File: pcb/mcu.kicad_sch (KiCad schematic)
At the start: 27 parts, among them SW1 PTS810, SW2 PTS810, U1 RP2040, U2 W25Q16JVSS, Y1 ABM8-272-T3

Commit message: add top level schem and cleanup
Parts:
- removed U1: RP2040, Package_DFN_QFN:QFN-56-1EP_7x7mm_P0.4mm_EP3.2x3.2mm, symbol MCU_RaspberryPi:RP2040
- removed U2: W25Q16JVSS, Package_SO:SOIC-8_5.3x5.3mm_P1.27mm, symbol Memory_Flash:W25Q16JVSS
- added U1: W25Q16JVSS, Package_SO:SOIC-8_5.3x5.3mm_P1.27mm, symbol Memory_Flash:W25Q16JVSS
- added U2: RP2040, Package_DFN_QFN:QFN-56-1EP_7x7mm_P0.4mm_EP3.2x3.2mm, symbol MCU_RaspberryPi:RP2040
- C1, C2: value 1u -> 100n; Manufacturer P/N GRM155Z71A105KE01J -> (none); Vendor DigiKey -> (none); Vendor P/N 490-GRM155Z71A105KE01JCT-ND -> (none)
- C11: value 100n -> 1u; Manufacturer P/N (none) -> GRM155Z71A105KE01J; Vendor (none) -> DigiKey; Vendor P/N (none) -> 490-GRM155Z71A105KE01JCT-ND
- C12: value 15p -> 1u; Manufacturer P/N GRM1555C1H150JA01D -> GRM155Z71A105KE01J; Vendor P/N 490-5888-1-ND -> 490-GRM155Z71A105KE01JCT-ND
- C13: value 15p -> 100n; Manufacturer P/N GRM1555C1H150JA01D -> (none); Vendor DigiKey -> (none); Vendor P/N 490-5888-1-ND -> (none)
- C4, C5: value 100n -> 15p; Manufacturer P/N (none) -> GRM1555C1H150JA01D; Vendor (none) -> DigiKey; Vendor P/N (none) -> 490-5888-1-ND
- R1: value 1k -> 10k; Manufacturer P/N RC0402FR-071KL -> RC0402FR-0710KL; Vendor P/N 311-1.00KLRCT-ND -> 311-10.0KLRCT-ND
- R2: value 10k -> 1k; Manufacturer P/N RC0402FR-0710KL -> RC0402FR-071KL; Vendor P/N 311-10.0KLRCT-ND -> 311-1.00KLRCT-ND; now fitted
- R3: value 1k -> 10k; Manufacturer P/N RC0402FR-071KL -> RC0402FR-0710KL; Vendor P/N 311-1.00KLRCT-ND -> 311-10.0KLRCT-ND; now not fitted
- R5: value 27.4 -> 1k; Manufacturer P/N RC0402FR-0727R4L -> RC0402FR-071KL; Vendor P/N YAG3085CT-ND -> 311-1.00KLRCT-ND
- R6: value 10k -> 27.4; Manufacturer P/N RC0402FR-0710KL -> RC0402FR-0727R4L; Vendor P/N 311-10.0KLRCT-ND -> YAG3085CT-ND
- R7, R8: value 2k -> 4.7k
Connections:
- net +1.1V: now also C12.1, C13.1, C14.1, U2.23 (DVDD), U2.45 (VREG_VOUT), U2.50 (DVDD); no longer C1.1, C3.1, C4.1
- net +3.3V: now also C1.1, C3.1, R1.2, R3.1, U1.8 (VCC), U2.1 (IOVDD), U2.10 (IOVDD), U2.22 (IOVDD), U2.33 (IOVDD), U2.42 (IOVDD), U2.43 (ADC_AVDD), U2.44 (VREG_VIN), U2.48 (USB_VDD), U2.49 (IOVDD); no longer C14.1, C5.1, R2.1, R6.2
- net GND: now also C12.2, C13.2, C4.1, C5.1, U1.4 (GND), U2.19 (TESTEN), U2.57 (GND); no longer C12.1, C13.1, C4.2, C5.2
- net I2C.SCL: now also U2.16 (GPIO13)
- net I2C.SDA: now also U2.15 (GPIO12)
- net QSPI_CLK: now also U1.6 (CLK), U2.52 (QSPI_SCLK)
- net QSPI_SD0: now also U1.5 (DI/IO_{0}), U2.53 (QSPI_SD0)
- net QSPI_SD1: now also U1.2 (DO/IO_{1}), U2.55 (QSPI_SD1)
- net QSPI_SD2: now also U1.3 (~{WP}/IO_{2}), U2.54 (QSPI_SD2)
- net QSPI_SD3: now also U1.7 (~{HOLD}/~{RESET}/IO_{3}), U2.51 (QSPI_SD3)
- net SWD.CLK: now also U2.24 (SWCLK)
- net SWD.DIO: now also U2.25 (SWDIO)
- net USB.DP: now also R6.1; no longer R5.1
- net gp_btn_a: now also U2.38 (GPIO26/ADC0)
- net gp_btn_b: now also U2.39 (GPIO27/ADC1)
- net gp_led_a: now also U2.40 (GPIO28/ADC2)
- net gp_led_b: now also U2.41 (GPIO29/ADC3)
- net hall_int: now also U2.2 (GPIO0)
- net ind_led0: now also U2.7 (GPIO5)
- net ind_led1: now also U2.8 (GPIO6)
- net ind_led2: now also U2.9 (GPIO7)
- net temp_int: now also U2.3 (GPIO1)
- net ~{QSPI_CS}: now also R2.1, R3.2, U1.1 (~{CS}), U2.56 (~{QSPI_SS}); no longer R2.2, R3.1
- net ~{RESET}: now also R1.1, U2.26 (RUN); no longer R6.1
- net ~{USB_BOOT}: now also R2.2; no longer R3.2
- net at Y1.1: now also C4.2, U2.20 (XIN); no longer C12.2
- net at R4.2: now also U2.46 (USB_DM)
- net at R5.2: now also C5.2, Y1.3
- new net: R5.1, U2.21 (XOUT)
- new net: R6.2, U2.47 (USB_DP)
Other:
- title: (none) -> MCU

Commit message: cleanup routing
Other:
- moved on the sheet: C1, R1, R2, R3, SW1, SW2, U1

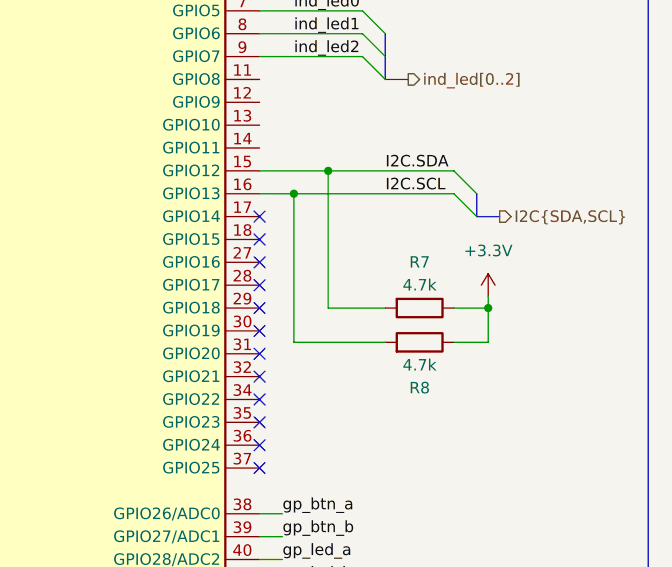
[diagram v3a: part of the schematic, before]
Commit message: custom symbols for all ics
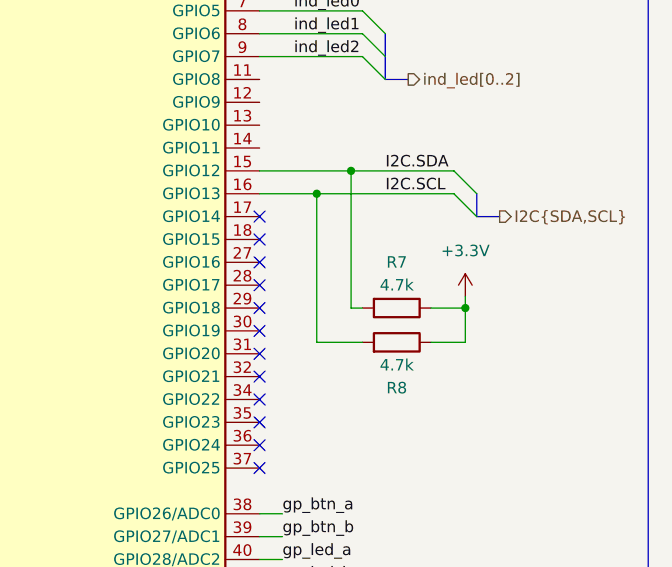
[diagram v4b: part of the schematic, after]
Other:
- moved on the sheet: R7, R8
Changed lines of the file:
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@@
 	)
 	(junction
-		(at 241.3 97.79)
+		(at 243.84 97.79)
 		(diameter 0)
 		(color 0 0 0 0)
@@
 	)
 	(junction
-		(at 237.49 100.33)
+		(at 240.03 100.33)
 		(diameter 0)
 		(color 0 0 0 0)
@@
 	)
 	(junction
-		(at 259.08 113.03)
+		(at 256.54 113.03)
 		(diameter 0)
 		(color 0 0 0 0)
@@
 	(wire
 		(pts
-			(xy 259.08 113.03) (xy 259.08 116.84)
+			(xy 256.54 113.03) (xy 256.54 116.84)
 		)
 		(stroke
@@
 	(wire
 		(pts
-			(xy 237.49 116.84) (xy 237.49 100.33)
+			(xy 240.03 116.84) (xy 240.03 100.33)
 		)
 		(stroke
@@
 	(wire
 		(pts
-			(xy 247.65 113.03) (xy 241.3 113.03)
+			(xy 245.11 113.03) (xy 243.84 113.03)
 		)
 		(stroke
@@
 	(wire
 		(pts
-			(xy 247.65 116.84) (xy 237.49 116.84)
+			(xy 245.11 116.84) (xy 240.03 116.84)
 		)
 		(stroke
@@
 	(wire
 		(pts
-			(xy 259.08 116.84) (xy 255.27 116.84)
+			(xy 256.54 116.84) (xy 252.73 116.84)
 		)
 		(stroke
@@
 	(wire
 		(pts
-			(xy 241.3 113.03) (xy 241.3 97.79)
+			(xy 243.84 113.03) (xy 243.84 97.79)
 		)
 		(stroke
@@
 	(wire
 		(pts
-			(xy 255.27 113.03) (xy 259.08 113.03)
+			(xy 252.73 113.03) (xy 256.54 113.03)
 		)
 		(stroke
@@
 	(wire
 		(pts
-			(xy 259.08 111.76) (xy 259.08 113.03)
+			(xy 256.54 111.76) (xy 256.54 113.03)
 		)
 		(stroke
@@
 	(symbol
 		(lib_id "Device:R")
-		(at 251.46 116.84 270)
+		(at 248.92 116.84 270)
 		(mirror x)
 		(unit 1)
@@
 		(dnp no)
 		(property "Reference" "R8"
-			(at 251.46 121.92 90)
+			(at 248.92 121.92 90)
 			(show_name no)
 			(do_not_autoplace no)
@@
 		)
 		(property "Value" "4.7k"
-			(at 251.46 119.38 90)
+			(at 248.92 119.38 90)
 			(show_name no)
 			(do_not_autoplace no)
@@
 		)
 		(property "Footprint" "Resistor_SMD:R_0402_1005Metric"
-			(at 251.46 118.618 90)
+			(at 248.92 118.618 90)
 			(hide yes)
 			(show_name no)
@@
 		)
 		(property "Datasheet" "https://yageogroup.com/content/datasheet/asset/file/PYU-RC_GROUP_51_ROHS_L"
-			(at 251.46 116.84 0)
+			(at 248.92 116.84 0)
 			(hide yes)
 			(show_name no)
@@
 		)
 		(property "Description" "1 kOhms ±1% 0.063W, 1/16W Chip Resistor 0402 (1005 Metric) Moisture Resistant Thick Film"
-			(at 251.46 116.84 0)
+			(at 248.92 116.84 0)
 			(hide yes)
 			(show_name no)
@@
 		)
 		(property "Manufacturer P/N" "RC0402FR-071KL"
-			(at 251.46 116.84 0)
+			(at 248.92 116.84 0)
 			(hide yes)
 			(show_name no)
@@
 		)
 		(property "Vendor" "DigiKey"
-			(at 251.46 116.84 0)
+			(at 248.92 116.84 0)
 			(hide yes)
 			(show_name no)
@@
 		)
 		(property "Vendor P/N" "311-1.00KLRCT-ND"
-			(at 251.46 116.84 0)
+			(at 248.92 116.84 0)
 			(hide yes)
 			(show_name no)
@@
 		)
 		(property "Manufaturer PIN" ""
-			(at 251.46 116.84 0)
+			(at 248.92 116.84 0)
 			(show_name no)
 			(do_not_autoplace no)
@@
 	(symbol
 		(lib_id "power:+3.3V")
-		(at 259.08 111.76 0)
+		(at 256.54 111.76 0)
 		(unit 1)
 		(body_style 1)
@@
 		(fields_autoplaced yes)
 		(property "Reference" "#PWR024"
-			(at 259.08 115.57 0)
+			(at 256.54 115.57 0)
 			(hide yes)
 			(show_name no)
@@
 		)
 		(property "Value" "+3.3V"
-			(at 259.08 106.68 0)
+			(at 256.54 106.68 0)
 			(show_name no)
 			(do_not_autoplace no)
@@
 		)
 		(property "Footprint" ""
-			(at 259.08 111.76 0)
+			(at 256.54 111.76 0)
 			(hide yes)
 			(show_name no)
@@
 		)
 		(property "Datasheet" ""
-			(at 259.08 111.76 0)
+			(at 256.54 111.76 0)
 			(hide yes)
 			(show_name no)
@@
 		)
 		(property "Description" "Power symbol creates a global label with name \"+3.3V\""
-			(at 259.08 111.76 0)
+			(at 256.54 111.76 0)
 			(hide yes)
 			(show_name no)
@@
 	(symbol
 		(lib_id "Device:R")
-		(at 251.46 113.03 270)
+		(at 248.92 113.03 270)
 		(unit 1)
 		(body_style 1)
@@
 		(dnp no)
 		(property "Reference" "R7"
-			(at 251.46 107.95 90)
+			(at 248.92 107.95 90)
 			(show_name no)
 			(do_not_autoplace no)
@@
 		)
 		(property "Value" "4.7k"
-			(at 251.46 110.49 90)
+			(at 248.92 110.49 90)
 			(show_name no)
 			(do_not_autoplace no)
@@
 		)
 		(property "Footprint" "Resistor_SMD:R_0402_1005Metric"
-			(at 251.46 111.252 90)
+			(at 248.92 111.252 90)
 			(hide yes)
 			(show_name no)
@@
 		)
 		(property "Datasheet" "https://yageogroup.com/content/datasheet/asset/file/PYU-RC_GROUP_51_ROHS_L"
-			(at 251.46 113.03 0)
+			(at 248.92 113.03 0)
 			(hide yes)
 			(show_name no)
@@
 		)
 		(property "Description" "1 kOhms ±1% 0.063W, 1/16W Chip Resistor 0402 (1005 Metric) Moisture Resistant Thick Film"
-			(at 251.46 113.03 0)
+			(at 248.92 113.03 0)
 			(hide yes)
 			(show_name no)
@@
 		)
 		(property "Manufacturer P/N" "RC0402FR-071KL"
-			(at 251.46 113.03 0)
+			(at 248.92 113.03 0)
 			(hide yes)
 			(show_name no)
@@
 		)
 		(property "Vendor" "DigiKey"
-			(at 251.46 113.03 0)
+			(at 248.92 113.03 0)
 			(hide yes)
 			(show_name no)
@@
 		)
 		(property "Vendor P/N" "311-1.00KLRCT-ND"
-			(at 251.46 113.03 0)
+			(at 248.92 113.03 0)
 			(hide yes)
 			(show_name no)
@@
 		)
 		(property "Manufaturer PIN" ""
-			(at 251.46 113.03 0)
+			(at 248.92 113.03 0)
 			(show_name no)
 			(do_not_autoplace no)

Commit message: Adding some docs
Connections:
- no-connect marks 17 -> 15
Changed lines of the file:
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@@
-	)
-	(no_connect
-		(at 233.68 69.85)
 	)
 	(no_connect
@@
 	(no_connect
 		(at 233.68 123.19)
-	)
-	(no_connect
-		(at 233.68 67.31)
 	)
 	(no_connect
@@
 	(wire
 		(pts
-			(xy 233.68 67.31) (xy 242.57 67.31)
-		)
-		(stroke
-			(width 0)
-			(type default)
-		)
-	)
-	(wire
-		(pts
 			(xy 54.61 64.77) (xy 74.93 64.77)
 		)
@@
 	(wire
 		(pts
+			(xy 233.68 69.85) (xy 246.38 69.85)
+		)
+		(stroke
+			(width 0)
+			(type default)
+		)
+	)
+	(wire
+		(pts
 			(xy 210.82 57.15) (xy 210.82 38.1)
 		)
@@
 	(wire
 		(pts
-			(xy 233.68 69.85) (xy 242.57 69.85)
-		)
-		(stroke
-			(width 0)
-			(type default)
-		)
-	)
-	(wire
-		(pts
 			(xy 153.67 120.65) (xy 182.88 120.65)
 		)
@@
 		(pts
 			(xy 128.27 38.1) (xy 139.7 38.1)
+		)
+		(stroke
+			(width 0)
+			(type default)
+		)
+	)
+	(wire
+		(pts
+			(xy 233.68 67.31) (xy 246.38 67.31)
 		)
 		(stroke
@@
 		)
 	)
-	(label "temp_int"
-		(at 236.22 69.85 0)
-		(effects
-			(font
-				(size 1.27 1.27)
-			)
-			(justify left bottom)
-		)
-	)
 	(label "ind_led2"
 		(at 237.49 85.09 0)
@@
 	(label "ind_led1"
 		(at 237.49 82.55 0)
-		(effects
-			(font
-				(size 1.27 1.27)
-			)
-			(justify left bottom)
-		)
-	)
-	(label "hall_int"
-		(at 236.22 67.31 0)
 		(effects
 			(font
@@
 		)
 	)
+	(hierarchical_label "hall_int"
+		(shape input)
+		(at 246.38 67.31 0)
+		(effects
+			(font
+				(size 1.27 1.27)
+			)
+			(justify left)
+		)
+	)
+	(hierarchical_label "temp_int"
+		(shape input)
+		(at 246.38 69.85 0)
+		(effects
+			(font
+				(size 1.27 1.27)
+			)
+			(justify left)
+		)
+	)

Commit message: Adding docs for GPIO and Color and removing INT
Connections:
- net hall_int: no longer names the net of U2.2 (GPIO0)
- net temp_int: no longer names the net of U2.3 (GPIO1)
- no-connect marks 15 -> 21
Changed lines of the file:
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@@
 	(title_block
 		(title "MCU")
-		(date "2026-10-27")
+		(date "2026-10-28")
+		(rev "2")
 	)
 	(rectangle
@@
 	)
 	(no_connect
+		(at 233.68 90.17)
+	)
+	(no_connect
+		(at 233.68 69.85)
+	)
+	(no_connect
 		(at 233.68 115.57)
 	)
@@
 	)
 	(no_connect
+		(at 233.68 95.25)
+	)
+	(no_connect
 		(at 233.68 110.49)
 	)
@@
 	)
 	(no_connect
+		(at 233.68 67.31)
+	)
+	(no_connect
+		(at 233.68 87.63)
+	)
+	(no_connect
 		(at 233.68 102.87)
 	)
@@
 	(no_connect
 		(at 233.68 72.39)
+	)
+	(no_connect
+		(at 233.68 92.71)
 	)
 	(no_connect
@@
 	(wire
 		(pts
-			(xy 233.68 69.85) (xy 246.38 69.85)
-		)
-		(stroke
-			(width 0)
-			(type default)
-		)
-	)
-	(wire
-		(pts
 			(xy 210.82 57.15) (xy 210.82 38.1)
 		)
@@
 		(pts
 			(xy 128.27 38.1) (xy 139.7 38.1)
-		)
-		(stroke
-			(width 0)
-			(type default)
-		)
-	)
-	(wire
-		(pts
-			(xy 233.68 67.31) (xy 246.38 67.31)
 		)
 		(stroke
@@
 		)
 	)
-	(hierarchical_label "hall_int"
-		(shape input)
-		(at 246.38 67.31 0)
-		(effects
-			(font
-				(size 1.27 1.27)
-			)
-			(justify left)
-		)
-	)
-	(hierarchical_label "temp_int"
-		(shape input)
-		(at 246.38 69.85 0)
-		(effects
-			(font
-				(size 1.27 1.27)
-			)
-			(justify left)
-		)
-	)

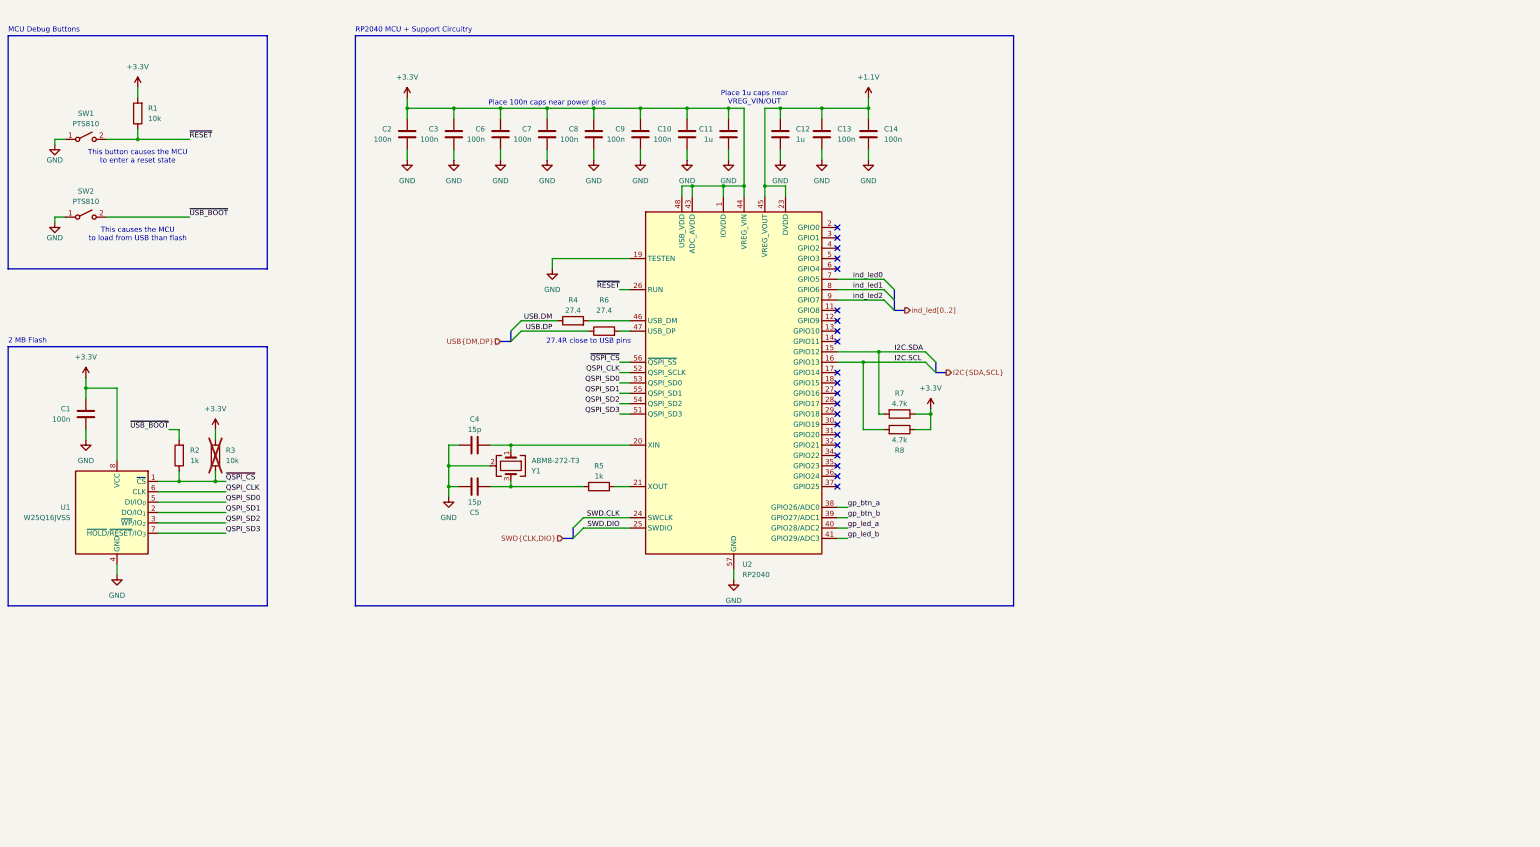
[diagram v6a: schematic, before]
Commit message: separate peripherals onto different i2c busses
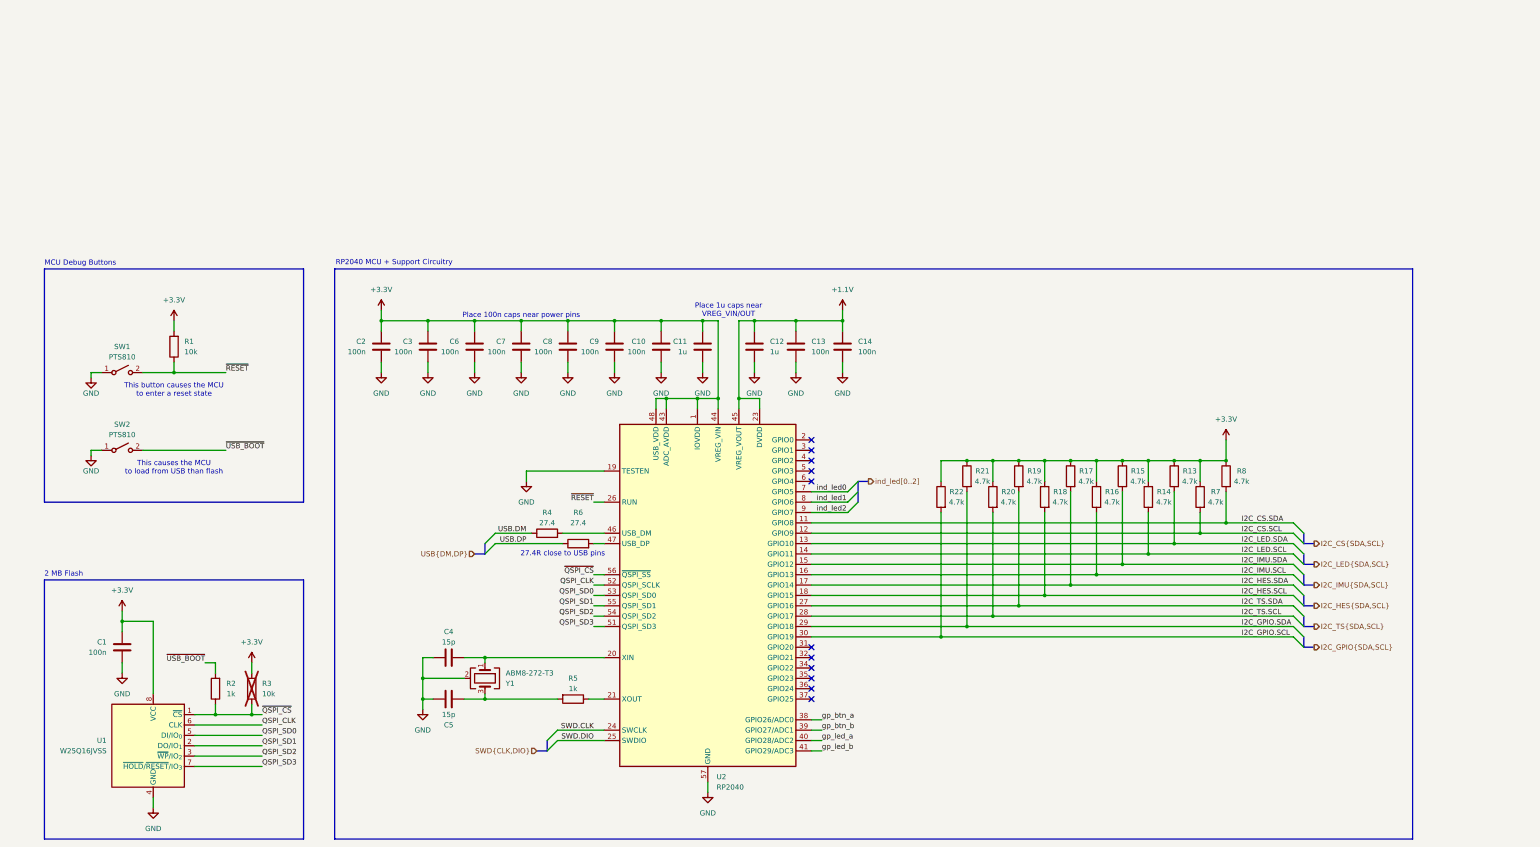
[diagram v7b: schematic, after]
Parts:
- added R13, R14, R15, R16, R17, R18, R19, R20, R21, R22: 4.7k, Resistor_SMD:R_0402_1005Metric, symbol Device:R
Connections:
- net +3.3V: now also R13.1, R14.1, R15.1, R16.1, R17.1, R18.1, R19.1, R20.1, R21.1, R22.1
- net I2C_CS.SDA: now reaches U2.11 (GPIO8)
- net I2C_CS.SDA: now also R8.2
- net I2C_CS.SCL: now reaches U2.12 (GPIO9)
- net I2C_CS.SCL: now also R7.2
- net I2C_LED.SDA: now reaches U2.13 (GPIO10)
- net I2C_LED.SDA: now also R13.2
- net I2C_LED.SCL: now reaches U2.14 (GPIO11)
- net I2C_LED.SCL: now also R14.2
- net I2C_HES.SDA: now reaches U2.17 (GPIO14)
- net I2C_HES.SDA: now also R17.2
- net I2C_HES.SCL: now reaches U2.18 (GPIO15)
- net I2C_HES.SCL: now also R18.2
- net I2C_TS.SDA: now reaches U2.27 (GPIO16)
- net I2C_TS.SDA: now also R19.2
- net I2C_TS.SCL: now reaches U2.28 (GPIO17)
- net I2C_TS.SCL: now also R20.2
- net I2C_GPIO.SDA: now reaches U2.29 (GPIO18)
- net I2C_GPIO.SDA: now also R21.2
- net I2C_GPIO.SCL: now reaches U2.30 (GPIO19)
- net I2C_GPIO.SCL: now also R22.2
- net I2C.SCL renamed I2C_IMU.SCL
- net I2C_IMU.SCL: now also R16.2; no longer R8.2
- net I2C.SDA renamed I2C_IMU.SDA
- net I2C_IMU.SDA: now also R15.2; no longer R7.2
- no-connect marks 21 -> 11
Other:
- moved on the sheet: C1, C10, C11, C12, C13, C14, C2, C3, C4, C5, C6, C7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

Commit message: fix pwr input erc errors
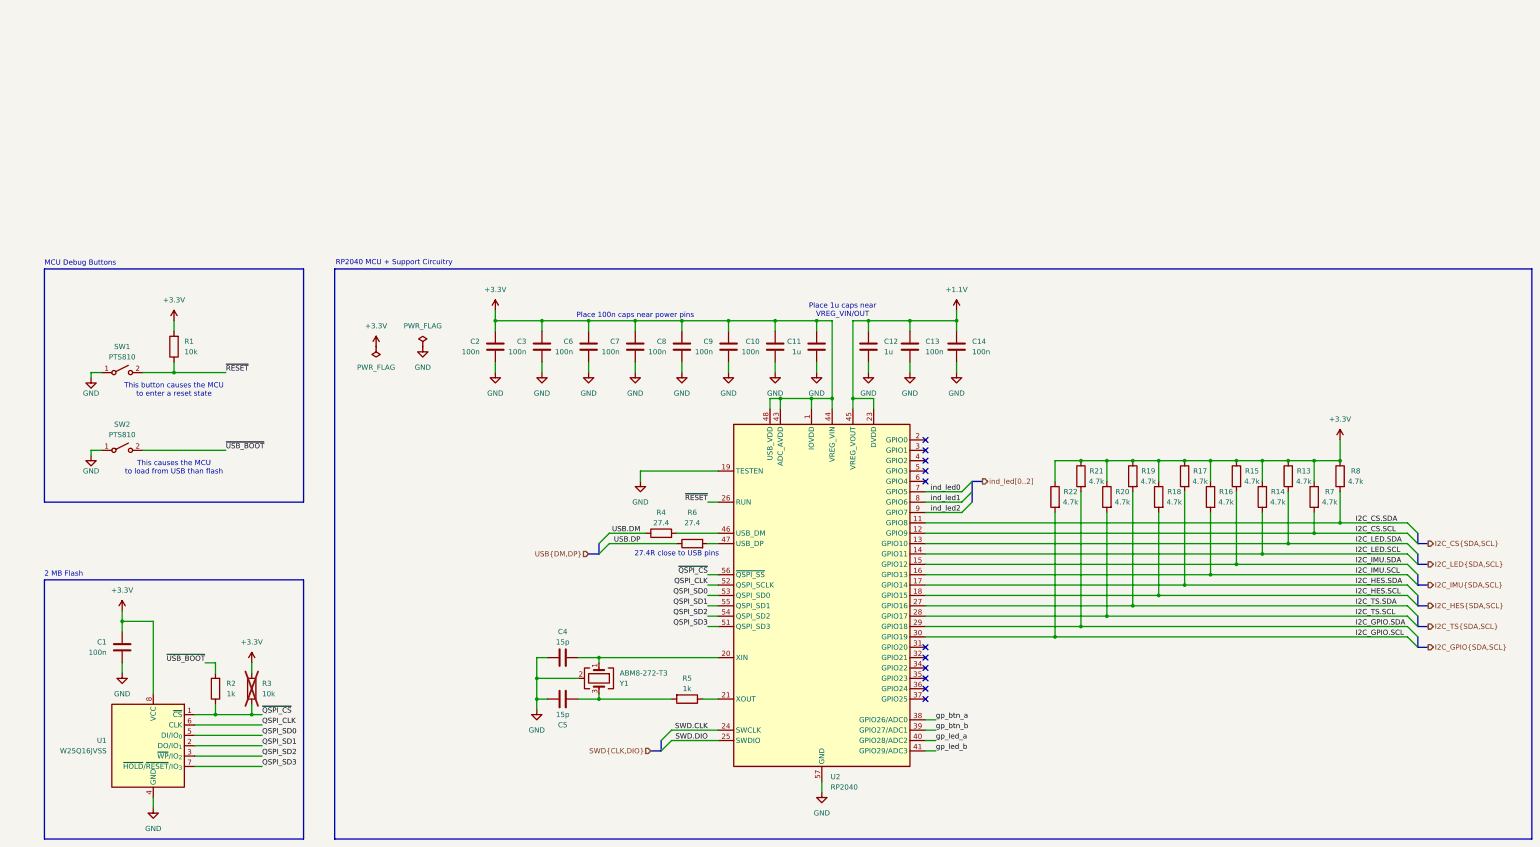
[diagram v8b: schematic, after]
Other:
- moved on the sheet: C10, C11, C12, C13, C14, C2, C3, C4, C5, C6, C7, C8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
